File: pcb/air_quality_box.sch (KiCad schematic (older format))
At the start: 10 parts, among them J1 MH-Z19B, J2 BME680, J3 SPS30, J4 ST7565, SW1 SW_SPDT, U1 NodeMCU_ESP8266

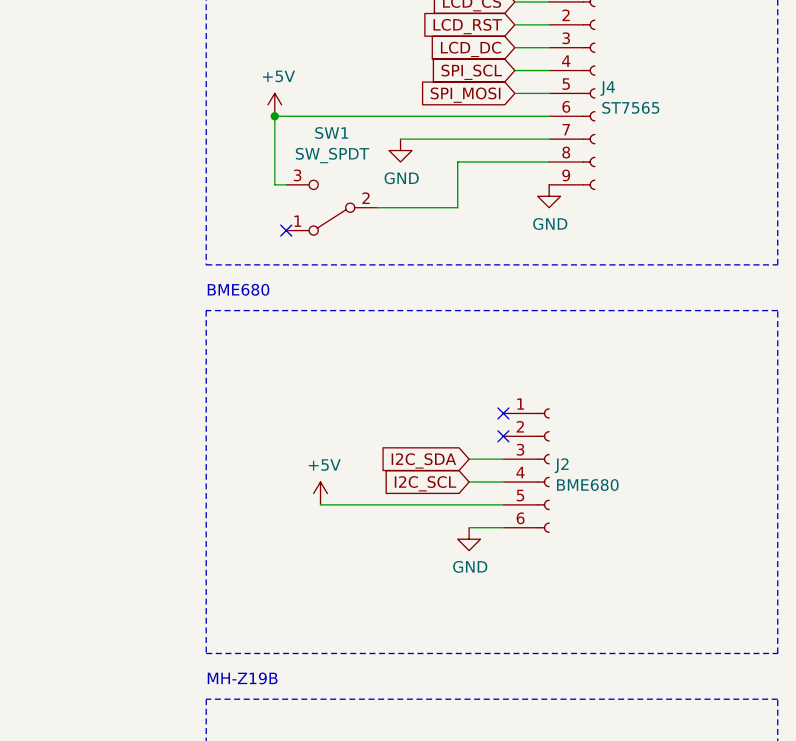
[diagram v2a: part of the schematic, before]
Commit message: Swap VCC and GNC pins on BME680
This mistake nearly cost me the sensor. To my luck only the regulator
released the magick smoke. After replacing the regulator the sensor
started working again.

Also, the screen diode draws a lot of current. Through experimentation I
figured out that it's bright enough with just 15mA of current. So I
added a 440 Ohm load in series with the backlight to limit the current
to about that value. This made also all sensor readings more stable, as
the MH-Z19 sensor draws up-to 100mA which brown-outs the MCU and other
sensors. Lowering the LCD current draw fixed that problem as well.
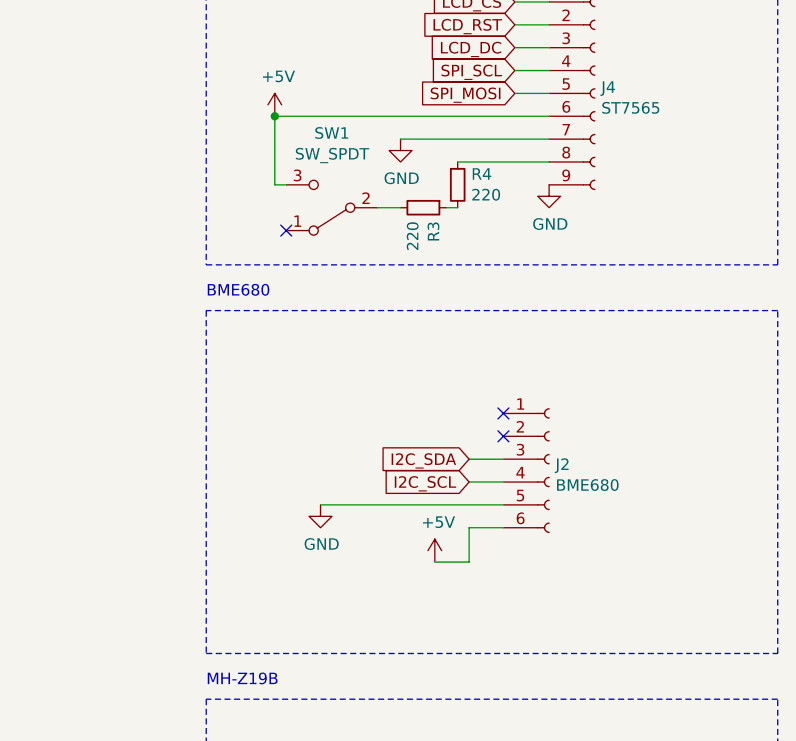
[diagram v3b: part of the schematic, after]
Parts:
- added R3, R4: 220, Resistor_THT:R_Axial_DIN0207_L6.3mm_D2.5mm_P10.16mm_Horizontal, symbol Device:R_Small
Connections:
- net +5V: now also J2.6 (Pin_6); no longer J2.5 (Pin_5)
- net GND: now also J2.5 (Pin_5); no longer J2.6 (Pin_6)
- net at J4.8 (Pin_8): now also R4.1; no longer SW1.2 (B)
- new net: R3.2, SW1.2 (B)
- new net: R3.1, R4.2
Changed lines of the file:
@@
 L power:+5V #PWR0103
 U 1 1 6179734D
+P 9500 3300
+F 0 "#PWR0103" H 9500 3150 50  0001 C CNN
+F 1 "+5V" H 9515 3473 50  0000 C CNN
+F 2 "" H 9500 3300 50  0001 C CNN
+F 3 "" H 9500 3300 50  0001 C CNN
+	1    9500 3300
+	1    0    0    -1
+$EndComp
+$Comp
+L power:GND #PWR0104
+U 1 1 61797AE0
 P 9000 3050
-F 0 "#PWR0103" H 9000 2900 50  0001 C CNN
-F 1 "+5V" H 9015 3223 50  0000 C CNN
+F 0 "#PWR0104" H 9000 2800 50  0001 C CNN
+F 1 "GND" H 9005 2877 50  0000 C CNN
 F 2 "" H 9000 3050 50  0001 C CNN
 F 3 "" H 9000 3050 50  0001 C CNN
 	1    9000 3050
-	1    0    0    -1
-$EndComp
-$Comp
-L power:GND #PWR0104
-U 1 1 61797AE0
-P 9650 3150
-F 0 "#PWR0104" H 9650 2900 50  0001 C CNN
-F 1 "GND" H 9655 2977 50  0000 C CNN
-F 2 "" H 9650 3150 50  0001 C CNN
-F 3 "" H 9650 3150 50  0001 C CNN
-	1    9650 3150
 	1    0    0    -1
 $EndComp
@@
 Wire Wire Line
 	10000 1550 9600 1550
-Wire Wire Line
-	9600 1550 9600 1750
-Wire Wire Line
-	9600 1750 9250 1750
 Wire Wire Line
 	8850 1650 8800 1650
@@
 	1    0    0    -1
 $EndComp
+Wire Wire Line
+	9500 3300 9650 3300
+Wire Wire Line
+	9650 3300 9650 3150
+$Comp
+L Device:R_Small R4
+U 1 1 61866701
+P 9600 1650
+F 0 "R4" H 9659 1696 50  0000 L CNN
+F 1 "220" H 9659 1605 50  0000 L CNN
+F 2 "Resistor_THT:R_Axial_DIN0207_L6.3mm_D2.5mm_P10.16mm_Horizontal" H 9600 1650 50  0001 C CNN
+F 3 "~" H 9600 1650 50  0001 C CNN
+	1    9600 1650
+	1    0    0    -1
+$EndComp
+$Comp
+L Device:R_Small R3
+U 1 1 61867248
+P 9450 1750
+F 0 "R3" H 9509 1796 50  0000 L CNN
+F 1 "220" H 9509 1705 50  0000 L CNN
+F 2 "Resistor_THT:R_Axial_DIN0207_L6.3mm_D2.5mm_P10.16mm_Horizontal" H 9450 1750 50  0001 C CNN
+F 3 "~" H 9450 1750 50  0001 C CNN
+	1    9450 1750
+	0    1    1    0
+$EndComp
+Wire Wire Line
+	9600 1750 9550 1750
+Wire Wire Line
+	9350 1750 9250 1750
 $EndSCHEMATC
